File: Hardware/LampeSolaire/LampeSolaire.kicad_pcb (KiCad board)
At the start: 2 copper layers, 85 x 75 mm, 52 parts, among them K1 RELAIS_DPDT, P1 1V8, P2 3V5, P3 3V5, P4 2V, T1 SI2333, T2 SI2333, T3 FDN337, T4 FDN337, T5 FDN337, T6 FDN337, T7 FDN337, U1 MCP73832, U2 MCP121, U3 NCP114ASN330T1G, U4 MRF89XAM8A, U5 PIC16F1827, U6 74xx00, X1 SOLAR_CELL, X2 ICSP, X4 BUZZER, X6 WATER_SENSOR

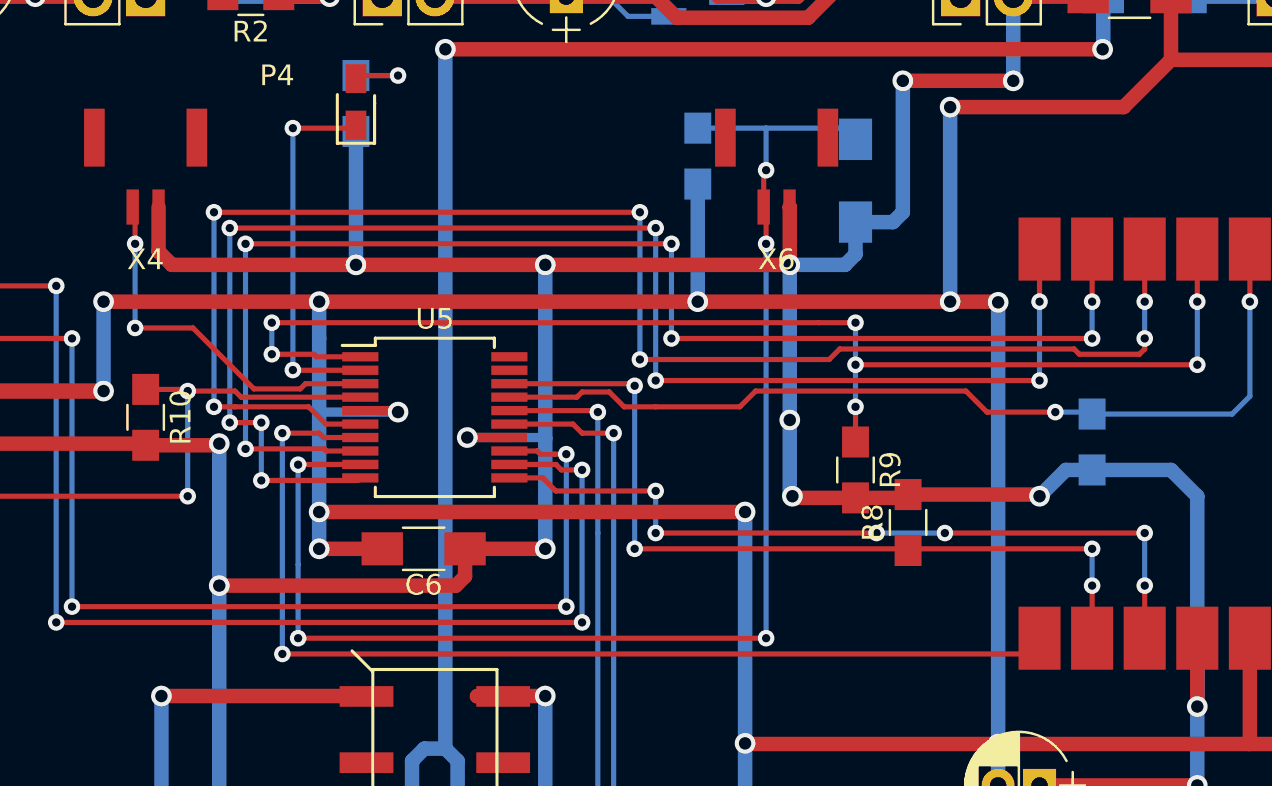
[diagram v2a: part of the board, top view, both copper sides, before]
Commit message: To remap because of error on ssop mcu
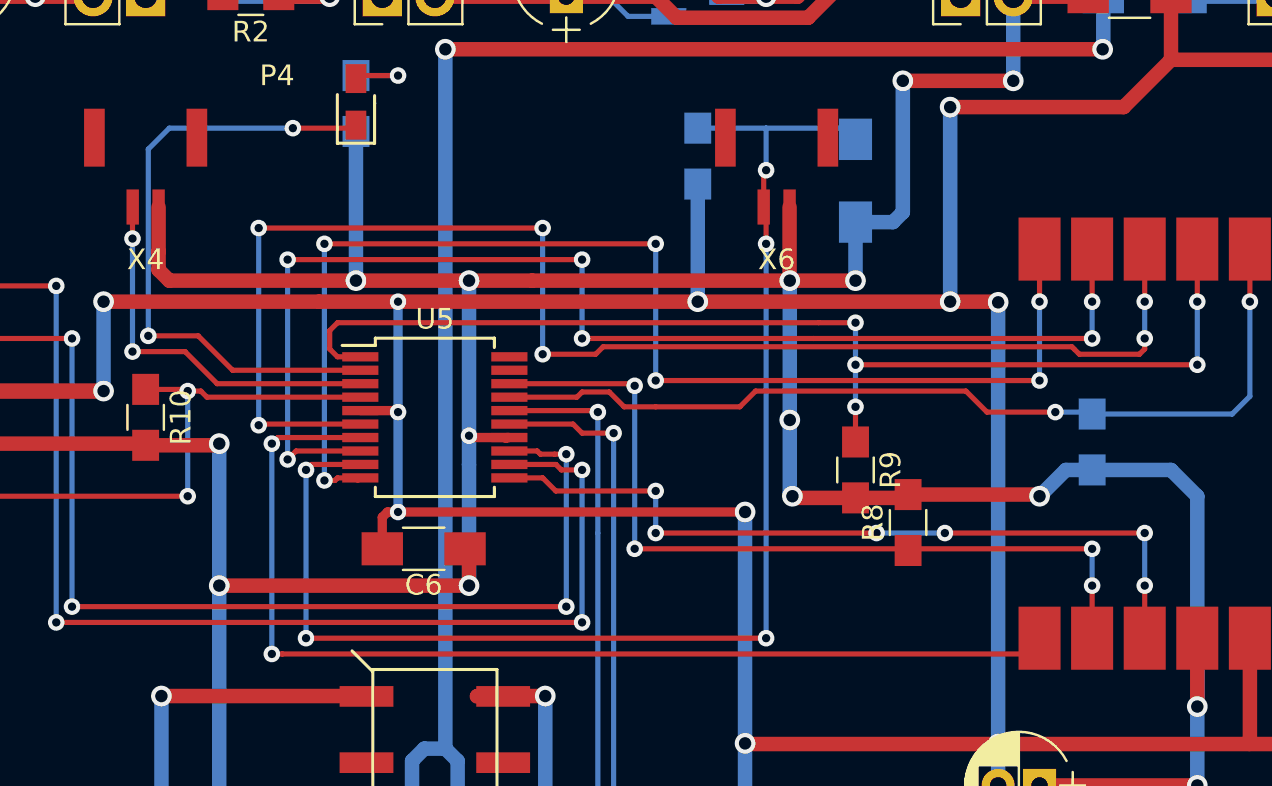
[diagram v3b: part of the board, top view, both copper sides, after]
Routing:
- net /LED: track 18.1 -> 30.5 mm
- net /SCK: track 71.4 -> 60.9 mm, vias 8 -> 6
- net GND: track 296.4 -> 286.4 mm, vias 18 -> 17
- net /~CSCON: track 61.9 -> 55.9 mm, vias 7 -> 5
- net /IRQ0: track 74.1 -> 68.6 mm
- net /MOSI: track 65.3 -> 60.3 mm
- net VCC: track 222.6 -> 219.7 mm, vias 16 -> 17
- net /WATER: track 66.6 -> 65.7 mm
- net /BUZZER: track 18.1 -> 18.6 mm
- net /MISO: track 51.4 -> 52.0 mm

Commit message: Remap complete
Commit before cleanup and size reducing
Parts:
- R8, R9: moved to B.Cu
- X2: footprint 0EsseivaN_Lib:Pin_Header_Angled_1x06_Pitch2.54mm -> 0EsseivaN_Lib:Pin_Header_Straight_1x06_Pitch2.54mm
- moved R8 2.91 mm to (110.2, 80.9)
- moved W4 2.91 mm to (126.0, 55.9), turned to 0 degrees
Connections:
- U5 pad 10: /SCK -> /WATER
- U5 pad 11: /IRQ1 -> /SCK
- U5 pad 12: /ICSPCLK -> /IRQ1
- U5 pad 13: /ICSPDAT -> /ICSPCLK
- U5 pad 14: VCC -> /ICSPDAT
- U5 pad 15: /RESET -> VCC
- U5 pad 16: /SET -> VCC
- U5 pad 17: /RESET_RF -> /RESET
- U5 pad 18: /~CSDATA -> /SET
- U5 pad 19: (no net) -> /RESET_RF
- U5 pad 20: (no net) -> /~CSDATA
- U5 pad 6: /IRQ0 -> GND
- U5 pad 7: /MISO -> /IRQ0
- U5 pad 8: /MOSI -> /MISO
- U5 pad 9: /WATER -> /MOSI
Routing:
- net GND: track 286.4 -> 260.2 mm, vias 17 -> 16
- net /SCK: track 60.9 -> 53.0 mm
- net /IRQ0: track 68.6 -> 64.5 mm
- net VCC: track 219.7 -> 223.6 mm, vias 17 -> 16
- net /~CSDATA: track 40.5 -> 44.2 mm, vias 4 -> 5
- net /SET: track 83.4 -> 86.7 mm
- net /WATER: track 65.7 -> 62.6 mm
- net /ICSPDAT: track 54.9 -> 57.6 mm
- net /MOSI: track 60.3 -> 58.2 mm
- net /MISO: track 52.0 -> 50.4 mm
- net /~CSCON: track 55.9 -> 57.2 mm, vias 5 -> 4
- net /IRQ1: track 38.1 -> 38.9 mm, vias 6 -> 4
- net GND_ALIM: track 125.5 -> 124.9 mm
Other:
- outline, holes or cut-outs redrawn

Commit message: Cleanup done
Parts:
- C6, R10: moved to B.Cu
- moved P4 23.3 mm to (73.3, 84.8), turned to 0 degrees
- moved R6 23.3 mm to (73.3, 84.8), turned to 180 degrees
- moved R5 17.8 mm to (100.0, 79.6)
- moved U4 17.8 mm to (103.8, 79.7)
- moved C8 15.2 mm to (91.1, 67.0), turned to 180 degrees
- moved C6 15.1 mm to (73.3, 75.9)
- moved R9 14.2 mm to (103.8, 67.0), turned to 180 degrees
- moved R8 13.5 mm to (101.4, 91.1), turned to 0 degrees
- moved U5 12.7 mm to (73.3, 78.4)
- moved C7 12.0 mm to (103.8, 100.0)
- moved X6 11.5 mm to (91.1, 67.0)
- moved R10 8.03 mm to (69.5, 70.8)
- moved R7 7.82 mm to (91.0, 64.4), turned to 0 degrees
- moved X4 7.73 mm to (79.7, 67.0)
- moved K1 1.27 mm to (84.8, 96.2)
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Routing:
- net GND: track 260.2 -> 230.2 mm, vias 16 -> 13
- net VCC: track 223.6 -> 196.8 mm, vias 16 -> 18
- net /SCK: track 53.0 -> 32.5 mm, vias 6 -> 4
- net /ICSPDAT: track 57.6 -> 44.9 mm
- net /ICSPCLK: track 59.4 -> 46.7 mm
- net /RESET: track 72.8 -> 60.1 mm, vias 4 -> 6
- net /LED: track 30.5 -> 19.5 mm
- net /SET: track 86.7 -> 97.5 mm
- net /~CSCON: track 57.2 -> 48.7 mm, vias 4 -> 1
- net /MISO: track 50.4 -> 42.8 mm
- net VBAT: track 93.2 -> 100.0 mm
- net /BUZZER: track 18.6 -> 25.2 mm
- net /MOSI: track 58.2 -> 52.1 mm
- net Net-(K1-Pad4): track 28.5 -> 34.6 mm
- net /RESET_RF: track 44.3 -> 38.2 mm, vias 2 -> 1
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- added copper zone on B.Cu, net GND
- added copper zone on B.Cu, net GND_ALIM
- added copper zone on F.Cu, net VCC
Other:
- board size 85 x 75 mm -> 83 x 75 mm
- board text added: "B.Cu - V5"
- board text added: "B.Mask - V5"
- board text added: "F.Cu - V5"
- board text added: "F.Mask - V5"
- board text added: "Lampe Solaire 26.04.19 - V5 EsseivaN"
- board text removed: "ALIM"
- board text removed: "B.Cu - V4"
- board text removed: "B.Mask - V4"
- board text removed: "CHARGE"
- board text removed: "F.Cu - V4"
- board text removed: "F.Mask - V4"
- board text removed: "LIGHT"
- board text removed: "LOGIC"
- board text removed: "Lampe Solaire 30.01.19 - V4 EsseivaN"
- board text removed: "RF"

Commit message: Ready for silks cleanup
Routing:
- added copper zone on F.Cu, net GND
- added copper zone on B.Cu, net VCC
- removed copper zone on B.Cu, net GND
- removed copper zone on F.Cu, net VCC
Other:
- board text added: "placer références"
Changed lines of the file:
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@@
   (general
     (thickness 1.6)
-    (drawings 78)
+    (drawings 79)
     (tracks 684)
     (zones 0)
@@
     (add_net VSC)
   )
+  (module 0EsseivaN_Lib:MRF89XAM8A (layer F.Cu)
+    (at 103.81 79.68 180)
+    (attr smd)
+    (fp_text reference U4 (at -8.866 0 270) (layer F.SilkS)
+      (effects (font (size 1 1) (thickness 0.15)))
+    )
+    (fp_text value MRF89XAM8A (at 0 0 180) (layer F.Fab)
+      (effects (font (size 1 1) (thickness 0.15)))
+    )
+    (fp_line (start 7.62 -6.858) (end 7.62 6.858) (layer F.SilkS) (width 0.15))
+    (fp_line (start -5.588 3.81) (end -4.826 2.794) (layer F.CrtYd) (width 0.12))
+    (fp_line (start -6.604 3.81) (end -4.826 1.524) (layer F.CrtYd) (width 0.12))
+    (fp_line (start -7.62 3.81) (end -4.826 0.254) (layer F.CrtYd) (width 0.12))
+    (fp_line (start -8.382 3.556) (end -4.826 -1.016) (layer F.CrtYd) (width 0.12))
+    (fp_line (start -8.382 2.54) (end -5.334 -1.524) (layer F.CrtYd) (width 0.12))
+    (fp_line (start -8.382 1.524) (end -6.096 -1.524) (layer F.CrtYd) (width 0.12))
+    (fp_line (start -8.382 0.508) (end -6.858 -1.524) (layer F.CrtYd) (width 0.12))
+    (fp_line (start -8.382 -0.508) (end -7.62 -1.524) (layer F.CrtYd) (width 0.12))
+    (fp_line (start -4.826 3.81) (end -8.382 3.81) (layer F.CrtYd) (width 0.12))
+    (fp_line (start -4.826 -1.524) (end -4.826 3.81) (layer F.CrtYd) (width 0.12))
+    (fp_line (start -8.382 -1.524) (end -4.826 -1.524) (layer F.CrtYd) (width 0.12))
+    (fp_line (start -8.382 3.81) (end -8.382 -1.524) (layer F.CrtYd) (width 0.12))
+    (fp_line (start -8.382 8.89) (end -8.382 -8.89) (layer F.CrtYd) (width 0.05))
+    (fp_line (start -20.32 -8.89) (end -20.32 8.89) (layer F.CrtYd) (width 0.05))
+    (fp_line (start 7.62 8.89) (end -20.32 8.89) (layer F.CrtYd) (width 0.05))
+    (fp_line (start 7.62 -8.89) (end 7.62 8.89) (layer F.CrtYd) (width 0.05))
+    (fp_line (start -20.32 -8.89) (end 7.62 -8.89) (layer F.CrtYd) (width 0.05))
+    (pad 6 smd rect (at 6.35 9.398 180) (size 2.032 3.048) (layers F.Cu F.Paste F.Mask)
+      (net 41 /SCK))
+    (pad 7 smd rect (at 6.35 -9.398 180) (size 2.032 3.048) (layers F.Cu F.Paste F.Mask)
+      (net 40 /MISO))
+    (pad 5 smd rect (at 3.81 9.398 180) (size 2.032 3.048) (layers F.Cu F.Paste F.Mask)
+      (net 39 /MOSI))
+    (pad 8 smd rect (at 3.81 -9.398 180) (size 2.032 3.048) (layers F.Cu F.Paste F.Mask)
+      (net 35 /~CSDATA))
+    (pad 4 smd rect (at 1.27 9.398 180) (size 2.032 3.048) (layers F.Cu F.Paste F.Mask)
+      (net 38 /IRQ0))
+    (pad 9 smd rect (at 1.27 -9.398 180) (size 2.032 3.048) (layers F.Cu F.Paste F.Mask)
+      (net 37 /IRQ1))
+    (pad 3 smd rect (at -1.27 9.398 180) (size 2.032 3.048) (layers F.Cu F.Paste F.Mask)
+      (net 36 /~CSCON))
+    (pad 10 smd rect (at -1.27 -9.398 180) (size 2.032 3.048) (layers F.Cu F.Paste F.Mask)
+      (net 4 VCC))
+    (pad 2 smd rect (at -3.81 9.398 180) (size 2.032 3.048) (layers F.Cu F.Paste F.Mask)
+      (net 43 /RESET_RF))
+    (pad 11 smd rect (at -3.81 -9.398 180) (size 2.032 3.048) (layers F.Cu F.Paste F.Mask)
+      (net 2 GND))
+    (pad 1 smd rect (at -6.35 9.398 180) (size 2.032 3.048) (layers F.Cu F.Paste F.Mask)
+      (net 2 GND))
+    (pad 12 smd rect (at -6.35 -9.398 180) (size 2.032 3.048) (layers F.Cu F.Paste F.Mask)
+      (net 2 GND))
+    (model C:/WorkSpace/_KicadLibraries/modules/packages3d/MRF89XAM8A.stp
+      (offset (xyz -6.096 0 0))
+      (scale (xyz 1 1 1))
+      (rotate (xyz -90 0 -90))
+    )
+  )
   (module 0EsseivaN_Lib:CP_Radial_D5.0mm_P2.00mm (layer F.Cu)
     (at 103.81 100 180)
@@
     )
   )
-  (module 0EsseivaN_Lib:MRF89XAM8A (layer F.Cu)
-    (at 103.81 79.68 180)
-    (attr smd)
-    (fp_text reference U4 (at -8.866 0 270) (layer F.SilkS)
-      (effects (font (size 1 1) (thickness 0.15)))
-    )
-    (fp_text value MRF89XAM8A (at 0 0 180) (layer F.Fab)
-      (effects (font (size 1 1) (thickness 0.15)))
-    )
-    (fp_line (start -4.826 3.81) (end -4.826 -1.524) (layer F.Fab) (width 0.12))
-    (fp_line (start -8.382 3.81) (end -4.826 3.81) (layer F.Fab) (width 0.12))
-    (fp_line (start -8.382 -1.524) (end -8.382 3.81) (layer F.Fab) (width 0.12))
-    (fp_line (start -4.826 -1.524) (end -8.382 -1.524) (layer F.Fab) (width 0.12))
-    (fp_line (start -8.382 -8.89) (end -8.382 8.89) (layer F.Fab) (width 0.12))
-    (fp_line (start 7.62 -8.89) (end -20.32 -8.89) (layer F.CrtYd) (width 0.12))
-    (fp_line (start -20.32 -8.89) (end -20.32 8.89) (layer F.CrtYd) (width 0.12))
-    (fp_line (start -20.32 8.89) (end 7.62 8.89) (layer F.CrtYd) (width 0.12))
-    (fp_line (start 7.62 8.89) (end 7.62 -8.89) (layer F.CrtYd) (width 0.12))
-    (pad 12 smd rect (at -6.35 -9.398 180) (size 2.032 3.048) (layers F.Cu F.Paste F.Mask)
-      (net 2 GND))
-    (pad 1 smd rect (at -6.35 9.398 180) (size 2.032 3.048) (layers F.Cu F.Paste F.Mask)
-      (net 2 GND))
-    (pad 11 smd rect (at -3.81 -9.398 180) (size 2.032 3.048) (layers F.Cu F.Paste F.Mask)
-      (net 2 GND))
-    (pad 2 smd rect (at -3.81 9.398 180) (size 2.032 3.048) (layers F.Cu F.Paste F.Mask)
-      (net 43 /RESET_RF))
-    (pad 10 smd rect (at -1.27 -9.398 180) (size 2.032 3.048) (layers F.Cu F.Paste F.Mask)
-      (net 4 VCC))
-    (pad 3 smd rect (at -1.27 9.398 180) (size 2.032 3.048) (layers F.Cu F.Paste F.Mask)
-      (net 36 /~CSCON))
-    (pad 9 smd rect (at 1.27 -9.398 180) (size 2.032 3.048) (layers F.Cu F.Paste F.Mask)
-      (net 37 /IRQ1))
-    (pad 4 smd rect (at 1.27 9.398 180) (size 2.032 3.048) (layers F.Cu F.Paste F.Mask)
-      (net 38 /IRQ0))
-    (pad 8 smd rect (at 3.81 -9.398 180) (size 2.032 3.048) (layers F.Cu F.Paste F.Mask)
-      (net 35 /~CSDATA))
-    (pad 5 smd rect (at 3.81 9.398 180) (size 2.032 3.048) (layers F.Cu F.Paste F.Mask)
-      (net 39 /MOSI))
-    (pad 7 smd rect (at 6.35 -9.398 180) (size 2.032 3.048) (layers F.Cu F.Paste F.Mask)
-      (net 40 /MISO))
-    (pad 6 smd rect (at 6.35 9.398 180) (size 2.032 3.048) (layers F.Cu F.Paste F.Mask)
-      (net 41 /SCK))
-  )
   (module 0EsseivaN_Lib:CP_Radial_D5.0mm_P2.00mm (layer F.Cu)
     (at 92.38 58.09 90)
@@
     )
   )
+  (gr_text "placer références" (at 126.5 110) (layer F.Cu)
+    (effects (font (size 3 3) (thickness 0.375)))
+  )
   (gr_text "Lampe Solaire\n26.04.19 - V5\nEsseivaN" (at 115.395 99.745) (layer B.SilkS)
     (effects (font (size 1.5 1.5) (thickness 0.3)) (justify mirror))
@@
     )
   )
-  (zone (net 2) (net_name GND) (layer B.Cu) (hatch edge 0.508)
+  (zone (net 4) (net_name VCC) (layer B.Cu) (hatch edge 0.508)
     (connect_pads (clearance 0.508))
     (min_thickness 0.6)
@@
     )
   )
-  (zone (net 4) (net_name VCC) (layer F.Cu) (hatch edge 0.508)
+  (zone (net 2) (net_name GND) (layer F.Cu) (hatch edge 0.508)
     (connect_pads (clearance 0.508))
     (min_thickness 0.6)
@@
       (pts
         (xy 112.5 64) (xy 112.5 60.5) (xy 57.5 60.5) (xy 57.5 119.5) (xy 105 119.5)
-        (xy 105 105.5) (xy 105 88.5) (xy 96 88.5) (xy 96 70.5) (xy 112.5 70.5)
+        (xy 105 105.5) (xy 112 105.5) (xy 112 94.5) (xy 112.5 94.5) (xy 112.5 70.5)
       )
     )

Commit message: V5 Complete
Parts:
- P2, P3, SC1, X4, X6: footprint 0EsseivaN_Lib:CH_2P -> 0EsseivaN_Lib:CH_02P
- PERC-4.5mm (x2): footprint MyLib:PERC-4.5mm -> 0EsseivaN_Lib:PERC-4.5mm
- SC2: renamed from X1; footprint 0EsseivaN_Lib:CH_2P -> 0EsseivaN_Lib:CH_02P
- V1: footprint 0EsseivaN_Lib:CH_3P -> 0EsseivaN_Lib:CH_03P
- moved SC1 1.27 mm to (72.1, 51.7)
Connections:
- net VCC renamed 3V3
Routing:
- net GND_ALIM: track 124.9 -> 123.1 mm
- net Net-(R4-Pad1): track 36.9 -> 38.6 mm
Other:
- board text added: "Lampe Solaire 28.04.19 - V5 EsseivaN"
- board text removed: "Lampe Solaire 26.04.19 - V5 EsseivaN"
- board text removed: "placer références"

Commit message: Update for next version
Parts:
- removed K1: RELAIS_DPDT, 0EsseivaN_Lib:Relay
- removed SC2: SOLAR_CELL, 0EsseivaN_Lib:CH_02P
- removed T4, T5, T6, T7: FDN337, 0EsseivaN_Lib:SOT-23_Handsoldering
- added C10: 4.7uF, 0EsseivaN_Lib:C_0805_HandSoldering, F.Cu at (74.6, 95.2)
- added C11: 100nF, Capacitors_SMD:C_1206_HandSoldering, B.Cu at (66.4, 63.5)
- added C9: 100nF, Capacitors_SMD:C_1206_HandSoldering, F.Cu at (85.4, 96.6)
- added U7: LD39200, 0EsseivaN_Lib:DFN-6-1EP_3x3mm_Pitch0.95mm, F.Cu at (79.7, 95.2)
- C1, C7: footprint 0EsseivaN_Lib:CP_Radial_D5.0mm_P2.00mm -> 0EsseivaN_Lib:C_0805_HandSoldering; moved to B.Cu
- P2, P3: value 3V5 -> 3V
- R12: value 22 -> 1k
- R5, R8, R9: value 1K -> 1k
- U6: value 74xx00 -> MCP9700; footprint 0EsseivaN_Lib:SOIC-14 -> 0EsseivaN_Lib:SOT-23_Handsoldering
- moved U6 49.3 mm to (67.0, 62.2), turned to 0 degrees
- moved R12 22.9 mm to (90.5, 87.7)
- moved P2 10.2 mm to (90.3, 101.3)
- moved P3 10.2 mm to (99.2, 101.3)
- moved R11 10.2 mm to (90.3, 103.8)
- moved R13 10.2 mm to (99.2, 103.8)
- moved C7 9.93 mm to (108.2, 91.1), turned to 0 degrees
- moved C1 8.12 mm to (68.2, 51.8), turned to 270 degrees
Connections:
- R11 pad 2: Net-(K1-Pad4) -> Net-(C10-Pad1)
- R12 pad 1: Net-(R12-Pad1) -> GND
- R12 pad 2: 3V3 -> /ENABLE
- R13 pad 2: Net-(K1-Pad5) -> Net-(C10-Pad1)
- U5 pad 17: /RESET -> /TEMP
- U5 pad 18: /SET -> /ENABLE
- U6 pad 1: /SET -> 3V3
- U6 pad 2: /SET -> /TEMP
- U6 pad 3: Net-(U6-Pad3) -> GND
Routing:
- net /SET: track 97.5 -> 0.00 mm, vias 6 -> 0
- net /RESET: track 60.1 -> 0.00 mm, vias 6 -> 0
- net /-: track 55.1 -> 0.00 mm, vias 4 -> 0
- net /+: track 49.6 -> 0.00 mm, vias 3 -> 0
- net Net-(C10-Pad1): track 0.00 -> 43.8 mm, vias 0 -> 3
- net Net-(K1-Pad4): track 34.6 -> 0.00 mm, vias 3 -> 0
- net /ENABLE: track 0.00 -> 33.4 mm, vias 0 -> 3
- net /TEMP: track 0.00 -> 32.5 mm, vias 0 -> 4
- net Net-(R12-Pad1): track 23.8 -> 0.00 mm, vias 2 -> 0
- net Net-(K1-Pad5): track 23.7 -> 0.00 mm, vias 1 -> 0
- net 3V3: track 196.8 -> 181.2 mm, vias 18 -> 19
- net /RESET2: track 15.5 -> 0.00 mm, vias 2 -> 0
- net VBAT: track 100.0 -> 86.7 mm, vias 4 -> 3
- net GND: track 230.0 -> 242.3 mm
- net Net-(SC1-Pad1): track 16.4 -> 6.21 mm, vias 2 -> 0
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- added copper zone on B.Cu, net GND
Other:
- board size 83 x 75 mm -> 83 x 64 mm
- net class Lamp removed
- net class alim_signals removed
- board text added: "B.Cu - V6"
- board text added: "B.Mask - V6"
- board text added: "F.Cu - V6"
- board text added: "F.Mask - V6"
- board text added: "Lampe Solaire 15.06.19 - V6 EsseivaN"
- board text removed: "B.Cu - V5"
- board text removed: "B.Mask - V5"
- board text removed: "F.Cu - V5"
- board text removed: "F.Mask - V5"
- board text removed: "Lampe Solaire 28.04.19 - V5 EsseivaN"
